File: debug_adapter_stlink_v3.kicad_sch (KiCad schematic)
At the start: 5 parts

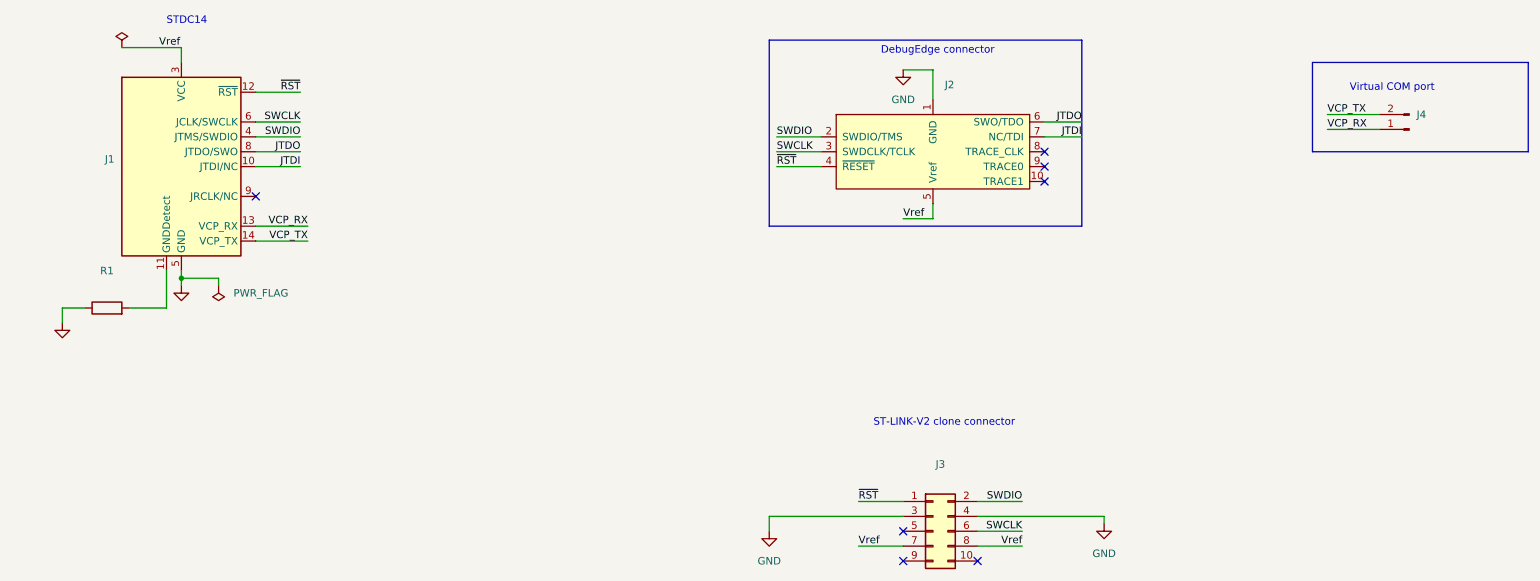
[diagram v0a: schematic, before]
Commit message: Remove the ST-Link-v2-clone connector
Reason: The adaptor for the ST-Link-V2 clone connector will be
implemented as its own PCB.
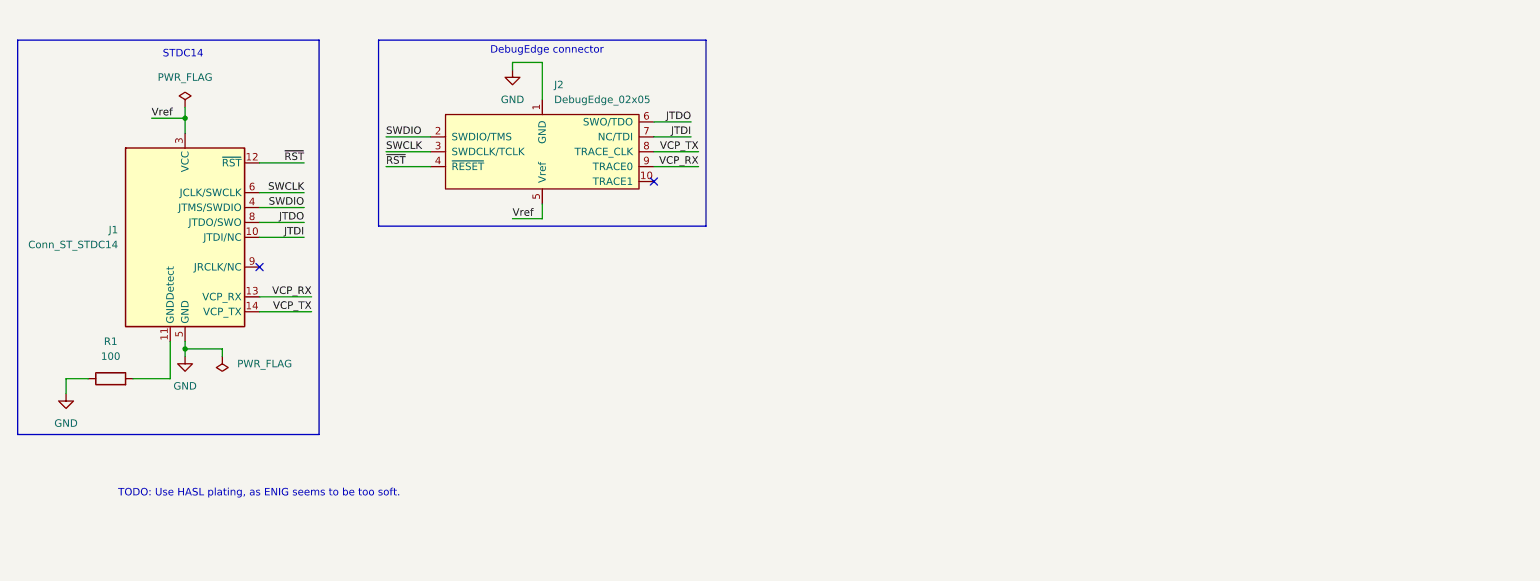
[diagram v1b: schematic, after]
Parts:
- removed J3: (no value), symbol Connector_Generic:Conn_02x05_Odd_Even
- removed J4: (no value), symbol Connector:Conn_01x02_Male
- J1: value (none) -> Conn_ST_STDC14; footprint (none) -> stdc14:cnc_tech_3221-14-0100-00
- J2: value (none) -> DebugEdge_02x05; footprint (none) -> DebugEdge:DebugEdge_2x05_Host
- R1: value (none) -> 100; footprint (none) -> Resistor_SMD:R_0805_2012Metric_Pad1.20x1.40mm_HandSolder
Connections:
- net VCP_RX: now also J2.9 (TRACE0)
- net VCP_TX: now also J2.8 (TRACE_CLK)
- no-connect marks 7 -> 2
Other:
- note added: "TODO: Use HASL plating, as ENIG seems to be too soft."
- note removed: "ST-LINK-V2 clone connector"
- note removed: "Virtual COM port"
- moved on the sheet: J1, J2, R1
